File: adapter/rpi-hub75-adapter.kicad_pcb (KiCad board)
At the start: 2 copper layers, 55 x 32 mm, 11 parts, among them P1 CONN_02X20, P2 CONN_01X02, P3 CONN_01X02, U1 74HC245, U2 74HC245, U3 74HC245

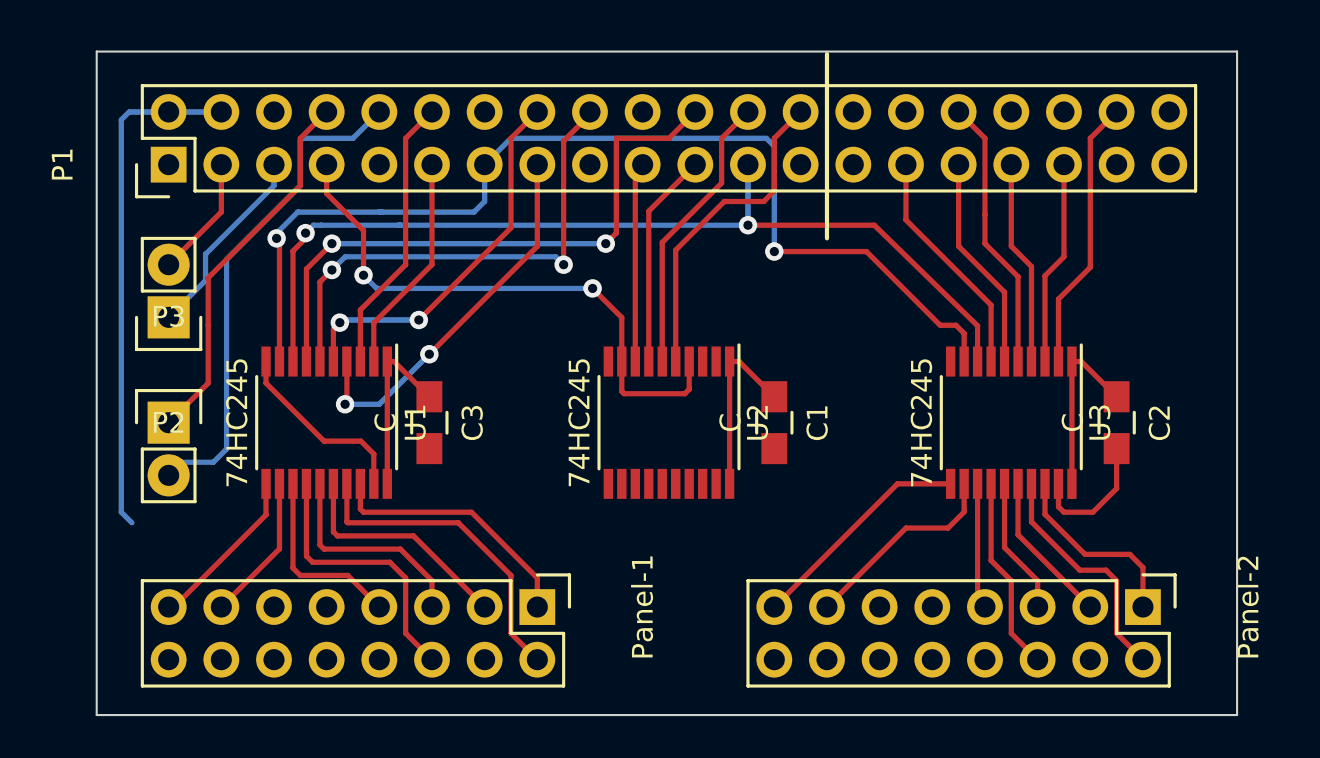
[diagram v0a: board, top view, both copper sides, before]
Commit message: o Better routing on left side.
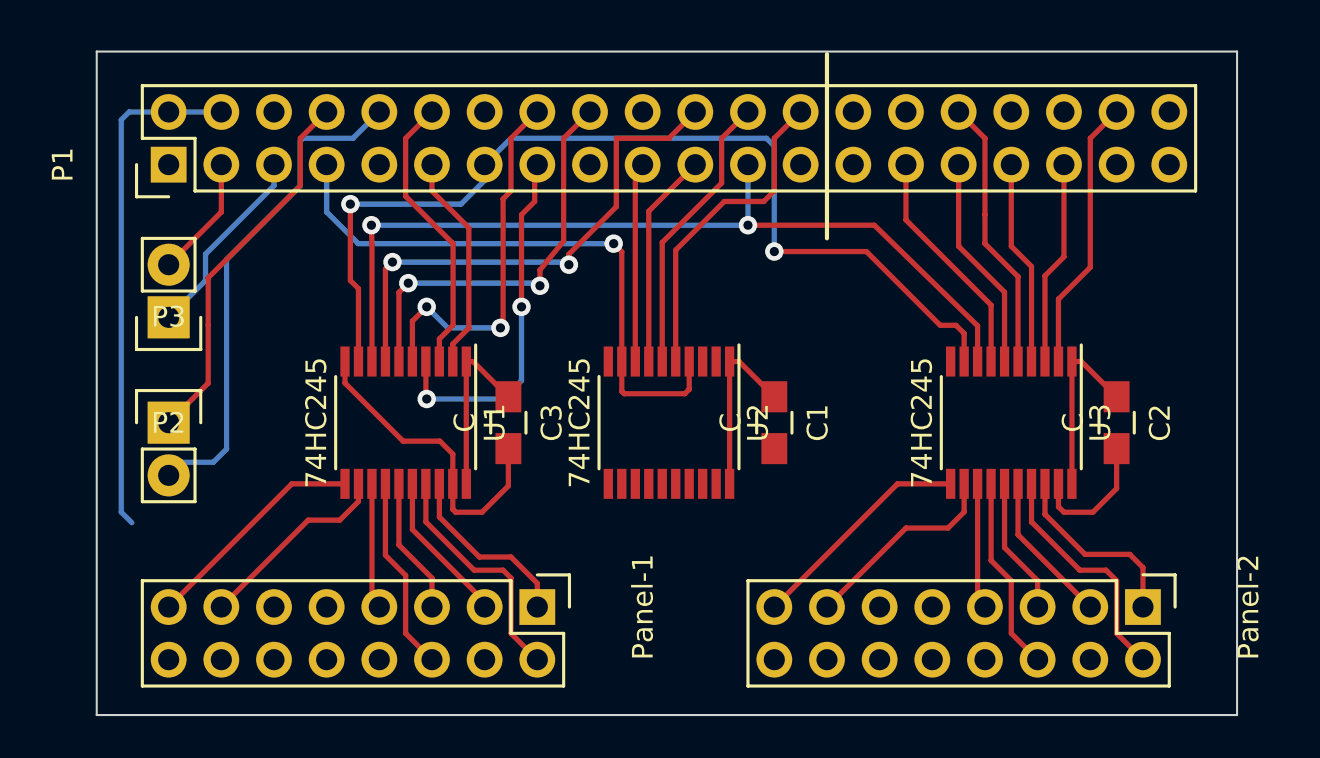
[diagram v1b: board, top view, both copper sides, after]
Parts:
- moved U1 3.81 mm to (88.9, 88.9)
- moved C3 3.81 mm to (93.9, 88.9)
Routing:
- net GND: track 16.0 -> 22.3 mm
- net p0_g2: track 24.5 -> 19.8 mm
- net p0_b2: track 29.0 -> 24.9 mm
- net p0_g1_buff: track 15.4 -> 11.5 mm
- net p0_g2_buff: track 13.2 -> 9.41 mm
- net Net-(Panel-1-Pad5): track 10.3 -> 6.60 mm
- net Net-(Panel-1-Pad1): track 12.5 -> 8.79 mm
- net Net-(Panel-1-Pad3): track 11.1 -> 7.38 mm
- net OE: track 50.7 -> 47.3 mm
- net clock: track 45.8 -> 42.4 mm
- net Net-(Panel-1-Pad15): track 8.03 -> 11.2 mm
- net Net-(Panel-1-Pad7): track 9.00 -> 6.09 mm
- net Net-(Panel-1-Pad13): track 7.10 -> 9.57 mm
- net strobe: track 27.7 -> 28.8 mm, vias 2 -> 1
- net p0_b1: track 18.5 -> 17.6 mm

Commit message: o Turning around the Hub75 connectors fits naturally the   way they want to be connected. Also: easier routing :)
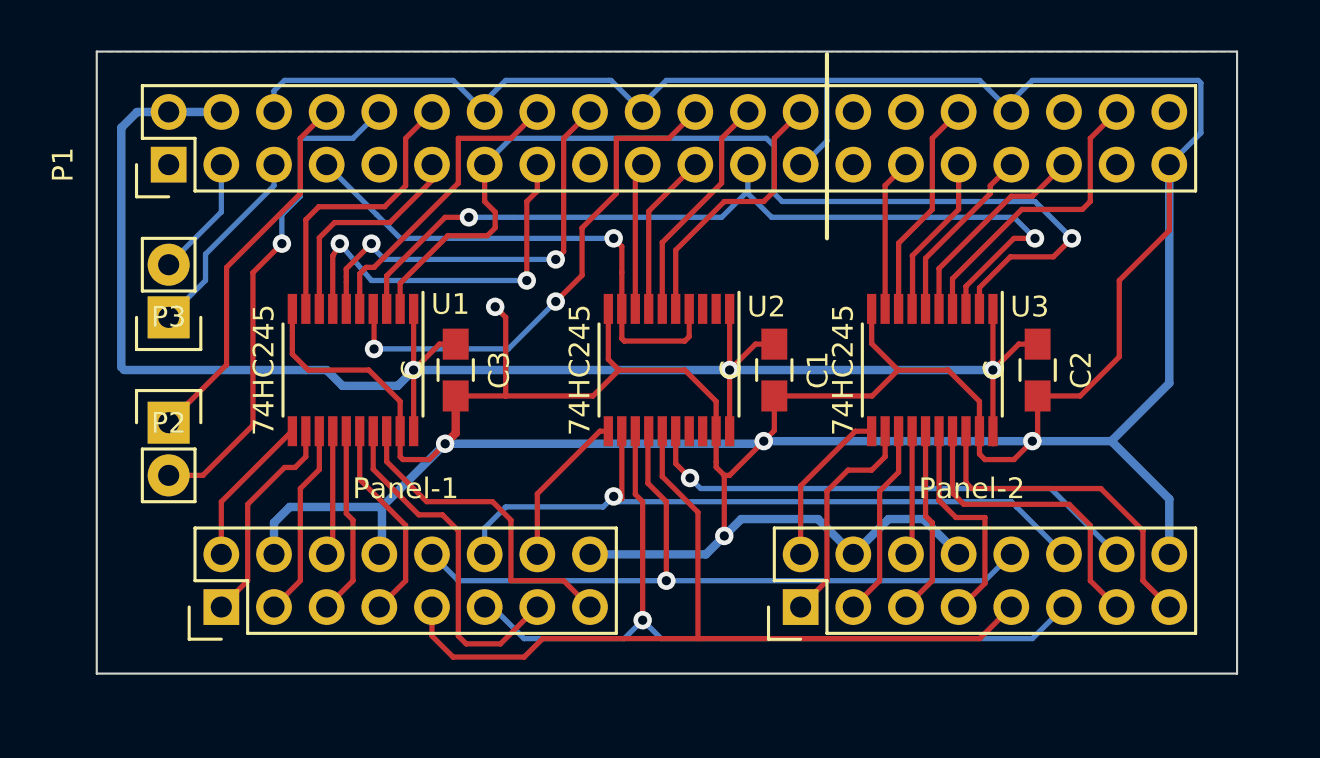
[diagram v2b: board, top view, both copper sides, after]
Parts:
- moved Panel-2 16.5 mm to (108.0, 97.8), turned to 90 degrees
- moved Panel-1 15.2 mm to (80.0, 97.8), turned to 90 degrees
- moved C2 4.58 mm to (119.4, 86.4)
- moved U3 4.58 mm to (114.3, 86.4)
- moved U1 3.59 mm to (86.4, 86.4)
- moved C3 3.59 mm to (91.3, 86.4)
- moved C1 2.54 mm to (106.7, 86.4)
- moved U2 2.54 mm to (101.6, 86.4)
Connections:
- net Net-(Panel-1-Pad5) renamed p0_r2_buff
- net Net-(Panel-2-Pad5) renamed p1_r2_buff
- P1 pad 29: p1_b2 -> p1_g1
- P1 pad 31: p1_g2 -> p1_b1
- P1 pad 32: p1_r2 -> p1_r1
- P1 pad 33: p1_b1 -> p1_g2
- P1 pad 35: p1_g1 -> p1_r2
- P1 pad 38: p1_r1 -> p1_b2
- Panel-1 pad 1: Net-(Panel-1-Pad1) -> p0_r1_buff
- Panel-1 pad 13: Net-(Panel-1-Pad13) -> clock_buff_0
- Panel-1 pad 15: Net-(Panel-1-Pad15) -> OE_buff_0
- Panel-1 pad 3: Net-(Panel-1-Pad3) -> p0_b1_buff
- Panel-1 pad 7: Net-(Panel-1-Pad7) -> p0_b2_buff
- Panel-2 pad 1: Net-(Panel-2-Pad1) -> p1_r1_buff
- Panel-2 pad 13: Net-(Panel-2-Pad13) -> clock_buff_1
- Panel-2 pad 15: Net-(Panel-2-Pad15) -> OE_buff_1
- Panel-2 pad 3: Net-(Panel-2-Pad3) -> p1_b1_buff
- Panel-2 pad 7: Net-(Panel-2-Pad7) -> p1_b2_buff
- U1 pad 11: Net-(Panel-1-Pad15) -> p0_g1_buff
- U1 pad 12: Net-(Panel-1-Pad13) -> p0_r1_buff
- U1 pad 13: Net-(Panel-1-Pad7) -> p0_b1_buff
- U1 pad 16: Net-(Panel-1-Pad3) -> p0_b2_buff
- U1 pad 17: p0_g1_buff -> clock_buff_0
- U1 pad 18: Net-(Panel-1-Pad1) -> OE_buff_0
- U1 pad 2: p0_r1 -> OE
- U1 pad 3: p0_g1 -> clock
- U1 pad 4: p0_b1 -> p0_b2
- U1 pad 7: p0_b2 -> p0_b1
- U1 pad 8: clock -> p0_r1
- U1 pad 9: OE -> p0_g1
- U3 pad 11: Net-(Panel-2-Pad15) -> p1_g1_buff
- U3 pad 12: Net-(Panel-2-Pad13) -> p1_r1_buff
- U3 pad 13: Net-(Panel-2-Pad7) -> p1_b1_buff
- U3 pad 16: Net-(Panel-2-Pad3) -> p1_b2_buff
- U3 pad 17: p1_g1_buff -> clock_buff_1
- U3 pad 18: Net-(Panel-2-Pad1) -> OE_buff_1
- U3 pad 2: p1_r1 -> OE
- U3 pad 3: p1_g1 -> clock
- U3 pad 4: p1_b1 -> p1_b2
- U3 pad 7: p1_b2 -> p1_b1
- U3 pad 8: clock -> p1_r1
- U3 pad 9: OE -> p1_g1
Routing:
- net GND: track 22.3 -> 234.5 mm, vias 0 -> 5
- net Net-(Panel-1-Pad9): track 0.00 -> 41.5 mm
- net Net-(Panel-1-Pad11): track 0.00 -> 39.2 mm, vias 0 -> 1
- net row_B_buff: track 0.00 -> 36.6 mm, vias 0 -> 1
- net row_D_buff: track 0.00 -> 34.7 mm, vias 0 -> 1
- net VCC: track 51.6 -> 85.9 mm, vias 0 -> 3
- net Net-(Panel-2-Pad14): track 0.00 -> 24.6 mm, vias 0 -> 1
- net clock_buff_0: track 0.00 -> 17.0 mm
- net OE_buff_1: track 0.00 -> 16.2 mm
- net OE_buff_0: track 0.00 -> 15.9 mm
- net clock_buff_1: track 0.00 -> 14.7 mm
- net Net-(Panel-1-Pad15): track 11.2 -> 0.00 mm
- net Net-(Panel-2-Pad15): track 11.0 -> 0.00 mm
- net p1_r1_buff: track 0.00 -> 10.8 mm
- net p1_b2_buff: track 0.00 -> 10.8 mm
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- added copper zone on B.Cu, net GND
- added copper zone on F.Cu, net GND
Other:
- board size 55 x 32 mm -> 55 x 30 mm
- net class Power added: clearance 0.508, trace_width 0.4064, via_dia 0.889, via_drill 0.635

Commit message: o More text..
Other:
- board text added: "Bottom Panel"
- board text added: "RxD"
- board text added: "SCL"
- board text added: "SDA"
- board text added: "Top Panel"
- board text added: "TxD"
- board text added: "github.com/hzeller/rpi-rgb-led-matrix"
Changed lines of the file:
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@@
     (area 68.953667 70.949999 129.050001 101.050001)
     (thickness 1.6)
-    (drawings 5)
+    (drawings 14)
     (tracks 429)
     (zones 0)
@@
     (visible_elements FFFFFF7F)
     (pcbplotparams
-      (layerselection 0x00030_80000001)
-      (usegerberextensions false)
+      (layerselection 0x010f0_80000001)
+      (usegerberextensions true)
       (excludeedgelayer true)
       (linewidth 0.100000)
@@
     (tags "SSOP 0.65")
     (attr smd)
-    (fp_text reference U1 (at -3.175 -4.699 360) (layer F.SilkS)
-      (effects (font (size 1 1) (thickness 0.15)))
-    )
-    (fp_text value 74HC245 (at 0 4.3 270) (layer F.SilkS)
+    (fp_text reference U1 (at -3.175 -4.445 450) (layer F.SilkS)
+      (effects (font (size 1 1) (thickness 0.15)))
+    )
+    (fp_text value 74HC245 (at -1.27 0 540) (layer F.SilkS)
       (effects (font (size 1 1) (thickness 0.15)))
     )
@@
     (tags "SSOP 0.65")
     (attr smd)
-    (fp_text reference U2 (at -3.048 -4.699 360) (layer F.SilkS)
-      (effects (font (size 1 1) (thickness 0.15)))
-    )
-    (fp_text value 74HC245 (at 0 4.3 270) (layer F.SilkS)
+    (fp_text reference U2 (at -3.175 -4.445 450) (layer F.SilkS)
+      (effects (font (size 1 1) (thickness 0.15)))
+    )
+    (fp_text value 74HC245 (at -1.27 0 360) (layer F.SilkS)
       (effects (font (size 1 1) (thickness 0.15)))
     )
@@
     (tags "SSOP 0.65")
     (attr smd)
-    (fp_text reference U3 (at -3.048 -4.699 360) (layer F.SilkS)
-      (effects (font (size 1 1) (thickness 0.15)))
-    )
-    (fp_text value 74HC245 (at 0 4.3 270) (layer F.SilkS)
+    (fp_text reference U3 (at -3.175 -4.445 450) (layer F.SilkS)
+      (effects (font (size 1 1) (thickness 0.15)))
+    )
+    (fp_text value 74HC245 (at -1.27 0 360) (layer F.SilkS)
       (effects (font (size 1 1) (thickness 0.15)))
     )
@@
     (descr "Through hole pin header")
     (tags "pin header")
-    (fp_text reference P1 (at 0 -5.1 90) (layer F.SilkS)
+    (fp_text reference P1 (at 1.524 -1.905 90) (layer F.SilkS)
       (effects (font (size 1 1) (thickness 0.15)))
     )
@@
     (descr "Through hole pin header")
     (tags "pin header")
-    (fp_text reference Panel-1 (at 5.715 8.89 180) (layer F.SilkS)
+    (fp_text reference Panel-1 (at 1.27 -2.54 270) (layer F.SilkS)
       (effects (font (size 1 1) (thickness 0.15)))
     )
@@
     (descr "Through hole pin header")
     (tags "pin header")
-    (fp_text reference Panel-2 (at 5.715 8.255 180) (layer F.SilkS)
+    (fp_text reference Panel-2 (at 1.27 -2.54 270) (layer F.SilkS)
       (effects (font (size 1 1) (thickness 0.15)))
     )
@@
     )
   )
+  (gr_line (start 86.995 100.33) (end 90.805 100.33) (angle 90) (layer F.SilkS) (width 1))
+  (gr_line (start 114.935 100.33) (end 118.745 100.33) (angle 90) (layer F.SilkS) (width 1))
+  (gr_text "Bottom Panel" (at 115.57 92.075) (layer F.SilkS)
+    (effects (font (size 1.5 1.5) (thickness 0.3)))
+  )
+  (gr_text "Top Panel" (at 89.535 92.075) (layer F.SilkS)
+    (effects (font (size 1.5 1.5) (thickness 0.3)))
+  )
+  (gr_text github.com/hzeller/rpi-rgb-led-matrix (at 104.775 81.28) (layer F.SilkS)
+    (effects (font (size 1.4 1.4) (thickness 0.3)))
+  )
+  (gr_text RxD (at 79.375 91.44) (layer F.SilkS)
+    (effects (font (size 1.5 1.2) (thickness 0.3)) (justify left))
+  )
+  (gr_text TxD (at 79.375 88.9) (layer F.SilkS)
+    (effects (font (size 1.5 1.2) (thickness 0.3)) (justify left))
+  )
+  (gr_text "SCL\n" (at 79.375 83.82) (layer F.SilkS)
+    (effects (font (size 1.5 1.2) (thickness 0.3)) (justify left))
+  )
+  (gr_text SDA (at 79.375 81.28) (layer F.SilkS)
+    (effects (font (size 1.5 1.2) (thickness 0.3)) (justify left))
+  )
   (gr_line (start 74 101) (end 74 71) (angle 90) (layer Edge.Cuts) (width 0.1))

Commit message: o Panel text
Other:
- board text added: "-> + and Pi2"
- board text added: "Pi 1 <-"

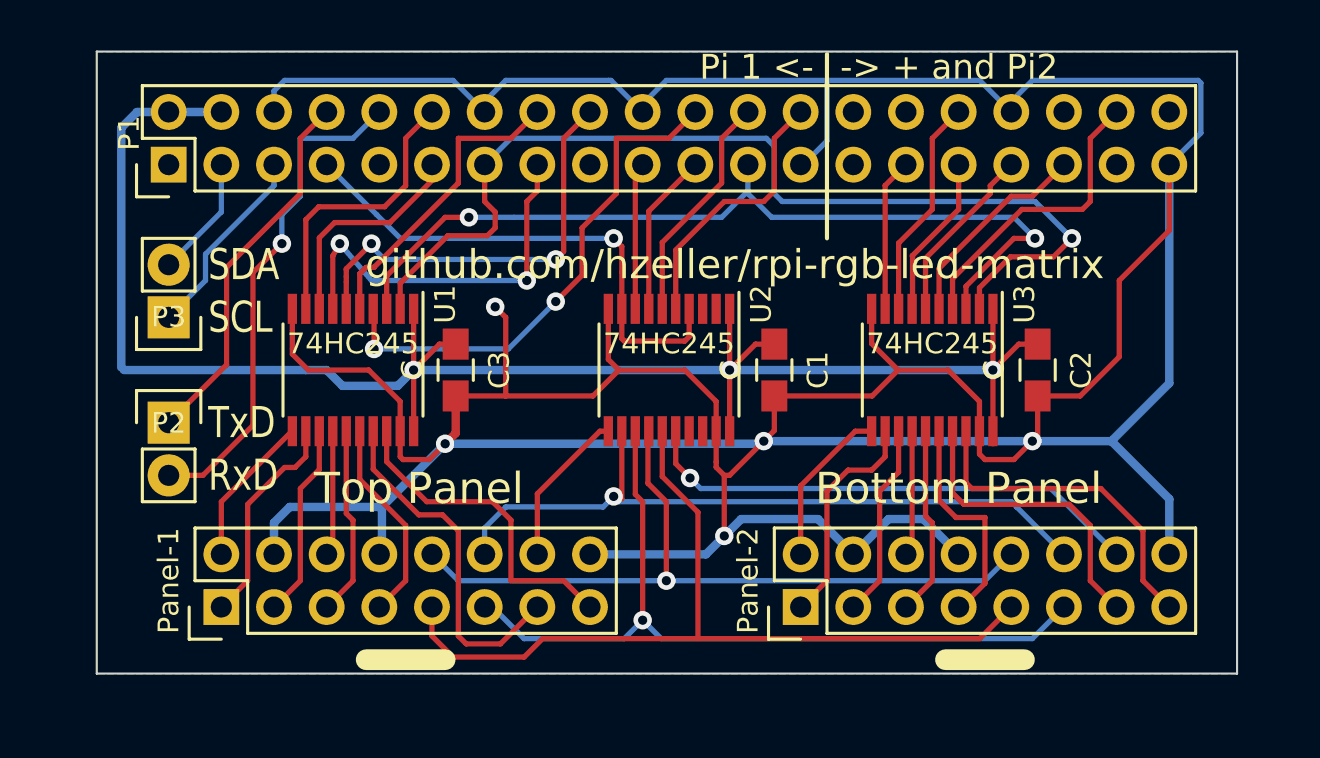
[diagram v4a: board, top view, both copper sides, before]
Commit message: o Make a bit more space for the IDC connector 'pocket'
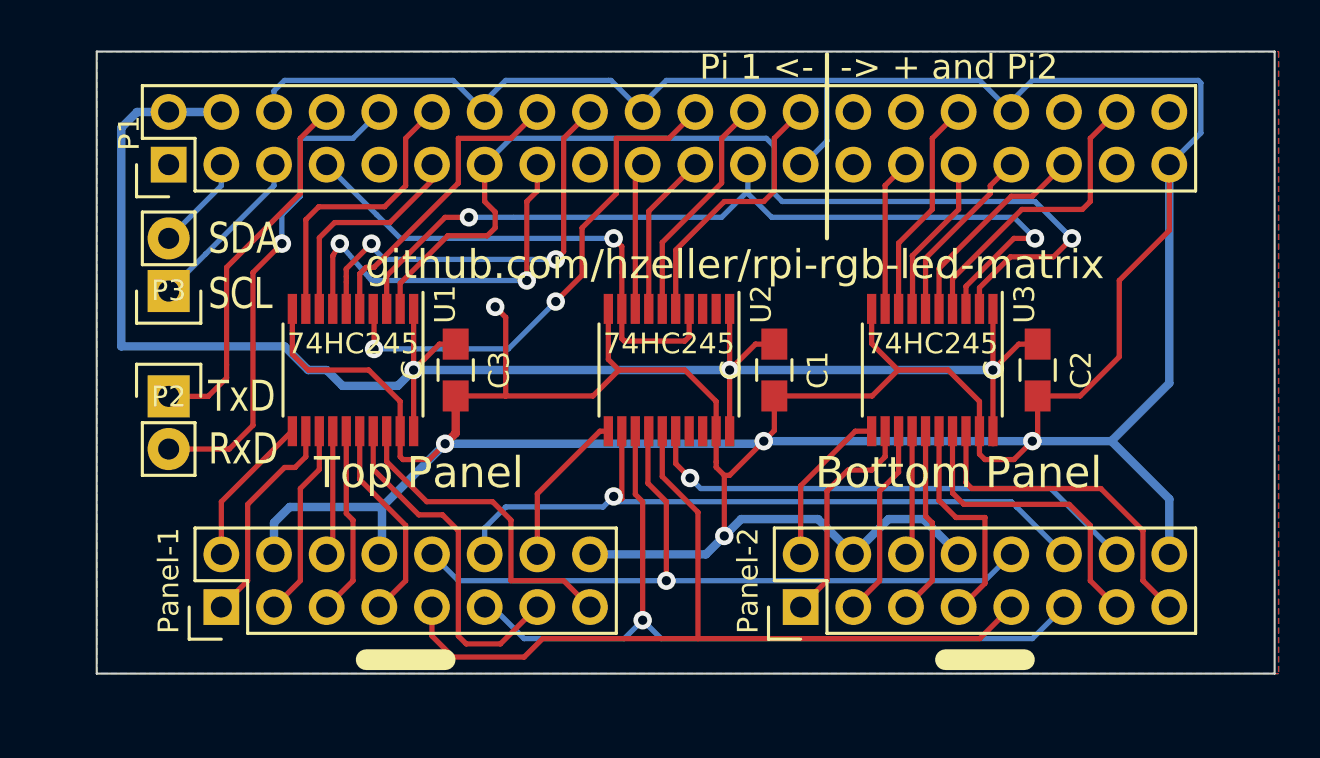
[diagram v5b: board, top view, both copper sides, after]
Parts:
- moved P3 1.27 mm to (77.5, 87.6)
- moved P2 1.27 mm to (77.5, 82.5)
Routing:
- net Net-(P1-Pad5): track 9.47 -> 8.20 mm
- net Net-(P1-Pad3): track 5.88 -> 4.61 mm
- net VCC: track 85.9 -> 85.3 mm
- net Net-(P1-Pad10): track 24.2 -> 23.7 mm
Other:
- board size 55 x 30 mm -> 56.8 x 30 mm
